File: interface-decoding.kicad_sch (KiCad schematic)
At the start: 1 part, among them U7 74HC32

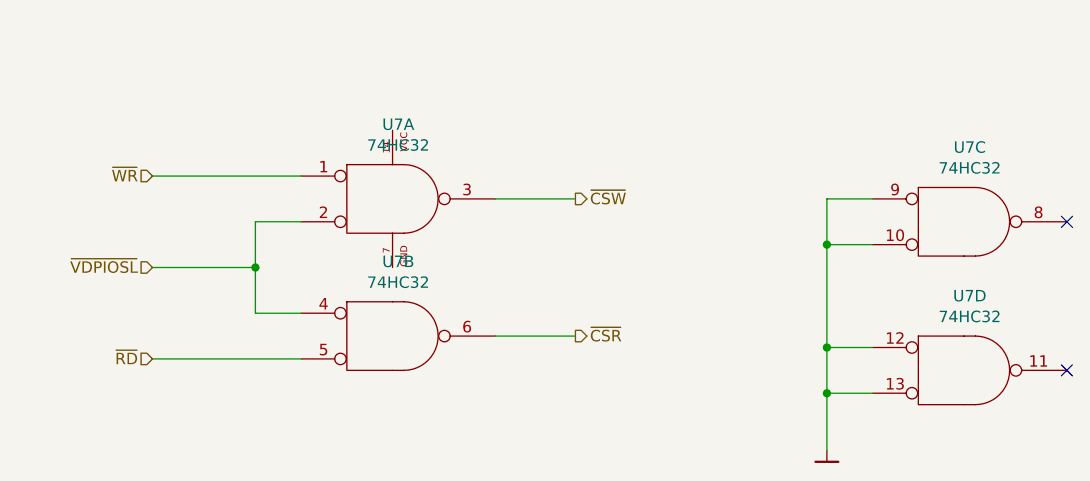
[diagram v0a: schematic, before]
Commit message: Update to latest Artemisa kicadlibs
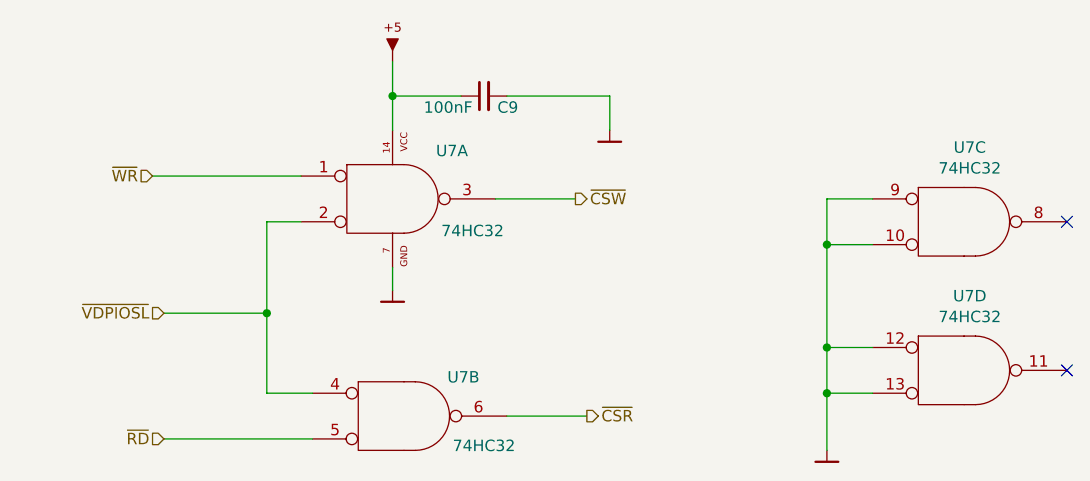
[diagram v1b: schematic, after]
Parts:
- added C9: 100nF, artemisa:Disc_capacitor, symbol artemisa:Cap
- U7: symbol artemisa:74HC32 -> PCM_artemisa:74HC32
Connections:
- net GND: now also U7.7 (GND), C9.2
- net VCC: now reaches U7.14 (VCC)
- net VCC: now also C9.1
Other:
- moved on the sheet: U7B

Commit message: Use spare MCP6294 as CSYNC buffer
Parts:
- C9: footprint artemisa:Disc_capacitor -> PCM_artemisa:Disc_capacitor
- U7: footprint artemisa:DIP-14_300 -> PCM_artemisa:DIP-14_300
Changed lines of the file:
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@@
 			)
 		)
-		(property "Footprint" "artemisa:DIP-14_300"
+		(property "Footprint" "PCM_artemisa:DIP-14_300"
 			(at 118.11 78.74 0)
 			(hide yes)
@@
 			)
 		)
-		(property "Footprint" "artemisa:DIP-14_300"
+		(property "Footprint" "PCM_artemisa:DIP-14_300"
 			(at 119.38 102.87 0)
 			(hide yes)
@@
 			)
 		)
-		(property "Footprint" "artemisa:DIP-14_300"
+		(property "Footprint" "PCM_artemisa:DIP-14_300"
 			(at 181.61 81.28 0)
 			(hide yes)
@@
 			)
 		)
-		(property "Footprint" "artemisa:DIP-14_300"
+		(property "Footprint" "PCM_artemisa:DIP-14_300"
 			(at 181.61 97.79 0)
 			(hide yes)
@@
 			)
 		)
-		(property "Footprint" "artemisa:Disc_capacitor"
+		(property "Footprint" "PCM_artemisa:Disc_capacitor"
 			(at 128.27 67.31 0)
 			(hide yes)
